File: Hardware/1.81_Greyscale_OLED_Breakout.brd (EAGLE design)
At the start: 15.2 x 63.5 mm, 26 parts, among them U1 AP3012, U2 3.3V, U3 TXB0104

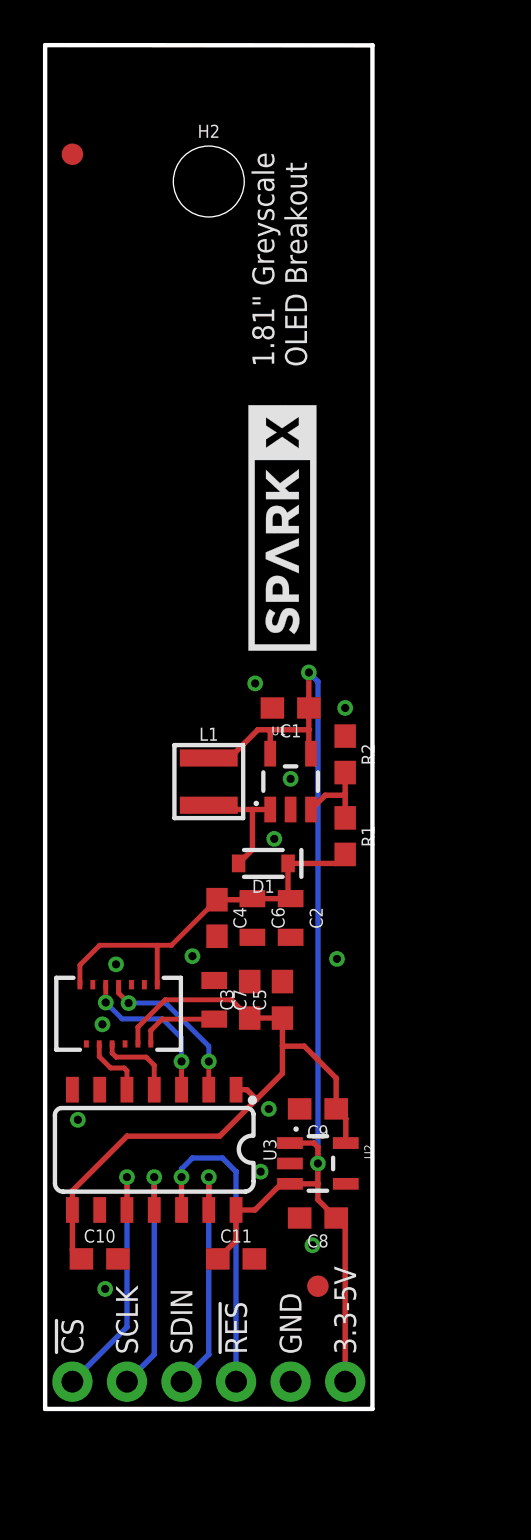
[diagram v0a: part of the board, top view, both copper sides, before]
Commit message: Made board smaller. Increased FPC footprint size.
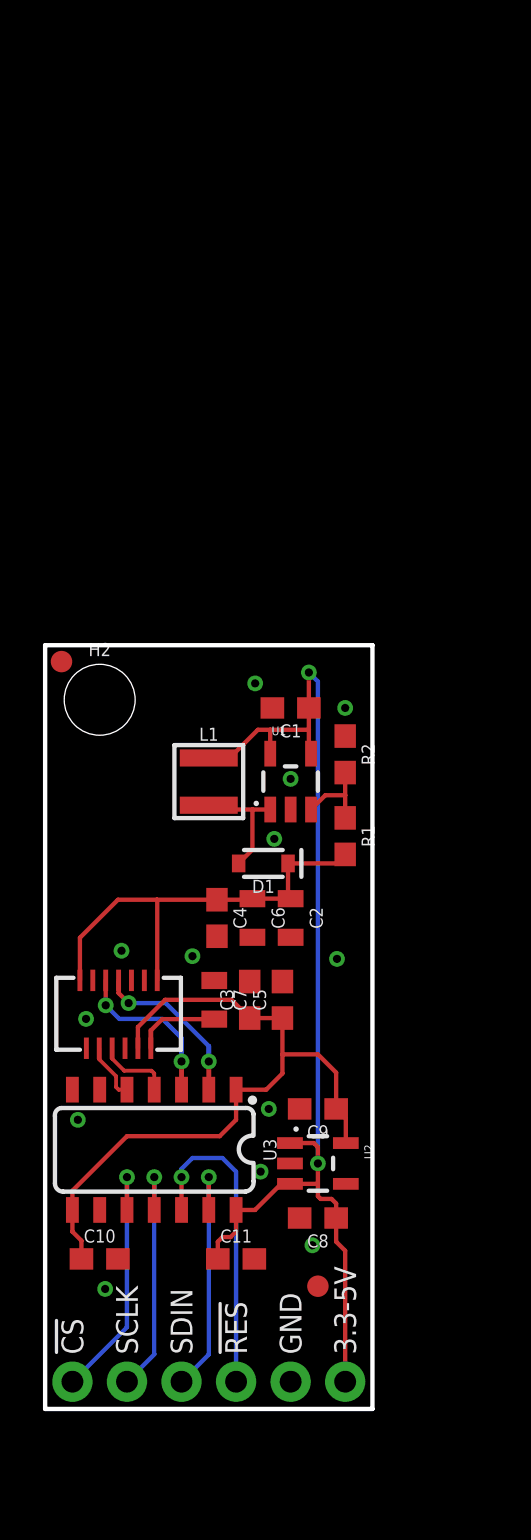
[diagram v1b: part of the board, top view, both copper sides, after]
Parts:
- removed LOGO2: SPARKX-LOGO5, 1.81_Greyscale_OLED_Breakout:SPARKX-XLARGE
- moved H2 24.7 mm to (2.54, 33.0)
- moved FD2 23.6 mm to (0.76, 34.8)
- moved LOGO1 18.1 mm to (7.49, 23.2), flipped to the bottom, turned to 0 degrees
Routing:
- net 12V: track 18.4 -> 20.8 mm
- net VIN: track 53.0 -> 53.5 mm
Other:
- board size 15.2 x 63.5 mm -> 15.2 x 35.6 mm
